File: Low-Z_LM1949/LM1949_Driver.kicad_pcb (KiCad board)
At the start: 2 copper layers, 37.5 x 27.3 mm, 16 parts, among them J1 Supply, J2 Input, J3 INJ_Out, Q1 BC817, Q2 TIP122, U1 LM1949N_NOPB

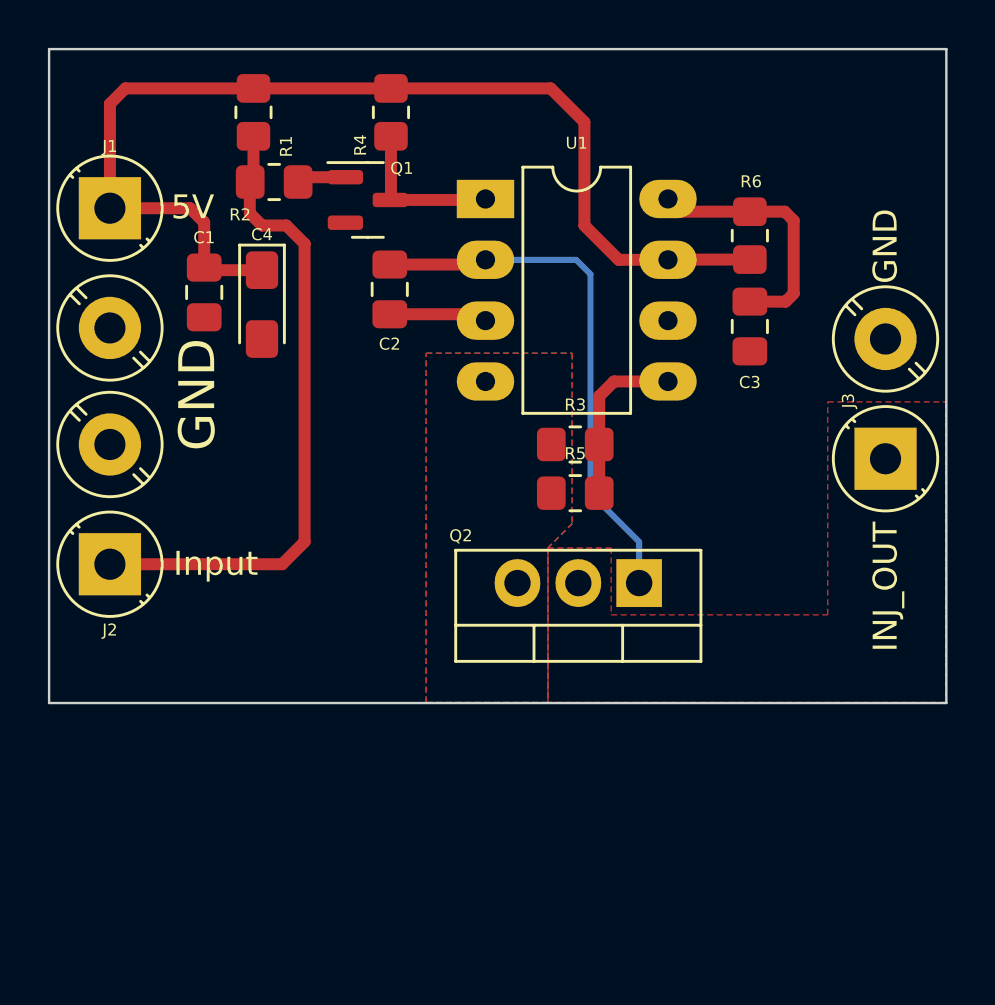
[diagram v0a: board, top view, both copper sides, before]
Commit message: revive or recreate LM1949 driver #173
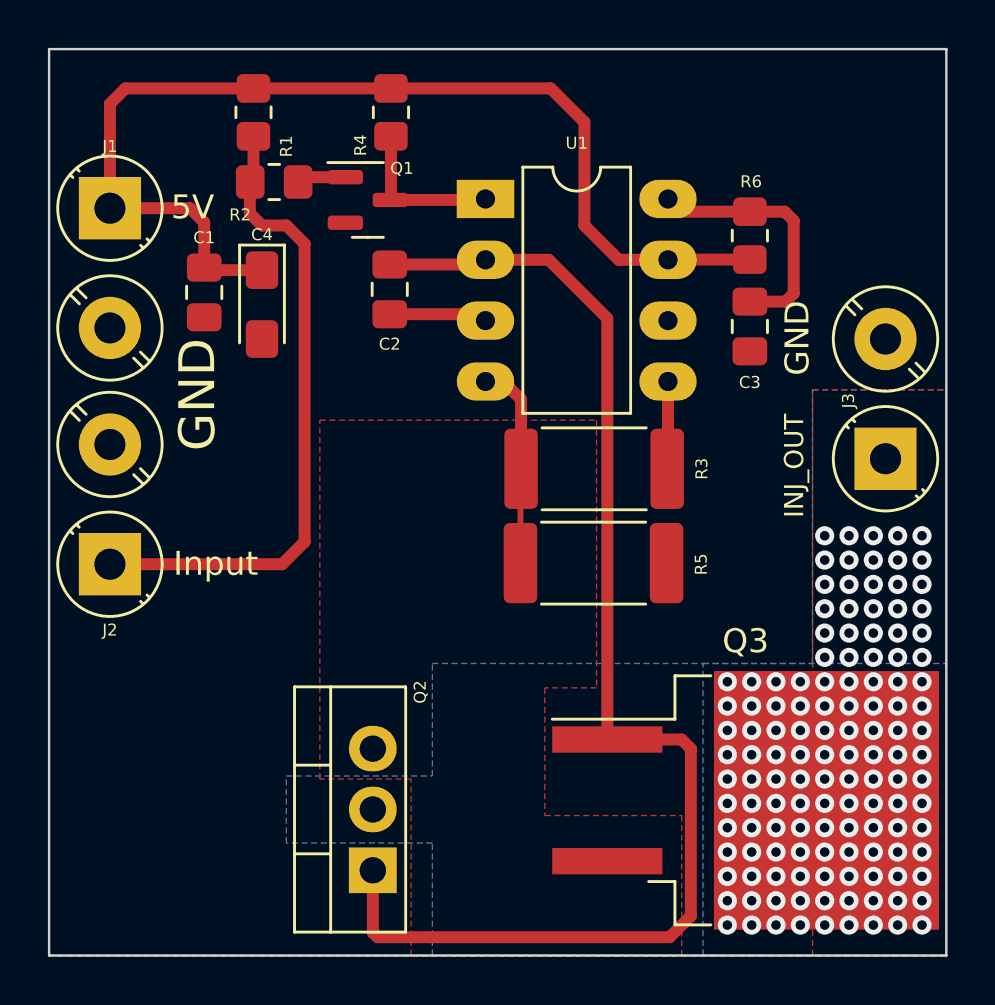
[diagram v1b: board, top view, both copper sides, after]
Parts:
- added Q3: FJB102TM, Package_TO_SOT_SMD:TO-263-2, F.Cu at (153.5, 80.9)
- R3, R5: value 0.22R -> 0.2R; footprint Resistor_SMD:R_0805_2012Metric_Pad1.20x1.40mm_HandSolder -> Resistor_SMD:R_2512_6332Metric_Pad1.40x3.35mm_HandSolder
- moved Q2 16.4 mm to (138.0, 83.8), turned to 90 degrees
- moved R5 3.02 mm to (147.2, 71.0)
- moved R3 1.29 mm to (147.2, 67.1)
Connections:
- net Net-(C2-Pad1) renamed /OUT
- net Net-(Q2-Pad2) renamed /INJ
- net Net-(Q2-Pad3) renamed /SEN
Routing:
- net /OUT: track 22.5 -> 54.7 mm
- net /SEN: track 0.00 -> 8.64 mm
- net GND: track 7.17 -> 3.66 mm
- net /INJ: vias 0 -> 129
- added copper zone on B.Cu, net /INJ
- removed copper zone on B.Cu, net /SEN
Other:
- board size 37.5 x 27.3 mm -> 37.5 x 37.8 mm
- board text added: "rusefi.com LM1949 rev 0.1"
